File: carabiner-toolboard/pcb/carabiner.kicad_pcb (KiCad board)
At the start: 2 copper layers, 32.1 x 35.5 mm, 24 parts, among them J1 MF-Vertical 43045-1612, J2 MF-Horizontal 43045-1621, J7 MF-Horizontal 43045-1600

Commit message: Carabiner R1.1 - 'Who even needs more pins?'
Duplicates Aux3 - this allows you to wire up a BLTouch much easier
Increase the maximum ampere for PCFs to 2A total
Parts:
- added JP_Aux3: SolderJumper_2_Open, Jumper:SolderJumper-2_P1.3mm_Open_TrianglePad1.0x1.5mm, B.Cu at (76.4, 66.5)
- Probe1: footprint Connector_JST:JST_XH_B4B-XH-A_1x04_P2.50mm_Vertical -> Connector_JST:JST_XH_B5B-XH-A_1x05_P2.50mm_Vertical
- renumbered JP_HEF_Alt1 to HEF_Alt, JP_HEF_Main1 to HEF_Main, JP_PCF_Alt1 to PCF_Alt, JP_PCF_Main1 to PCF_Main
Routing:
- net A3: track 21.6 -> 30.7 mm
- net Net-(JP_Aux3-Pad2): track 0.00 -> 3.91 mm
- net PcFanGnd: track 23.3 -> 21.2 mm
- net PcFanSwitch: track 11.9 -> 10.9 mm
- net AltVolt: track 30.7 -> 30.3 mm, vias 1 -> 0
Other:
- board text added: "Carabiner R1.1"
- board text removed: "Carabiner R1.0.1"

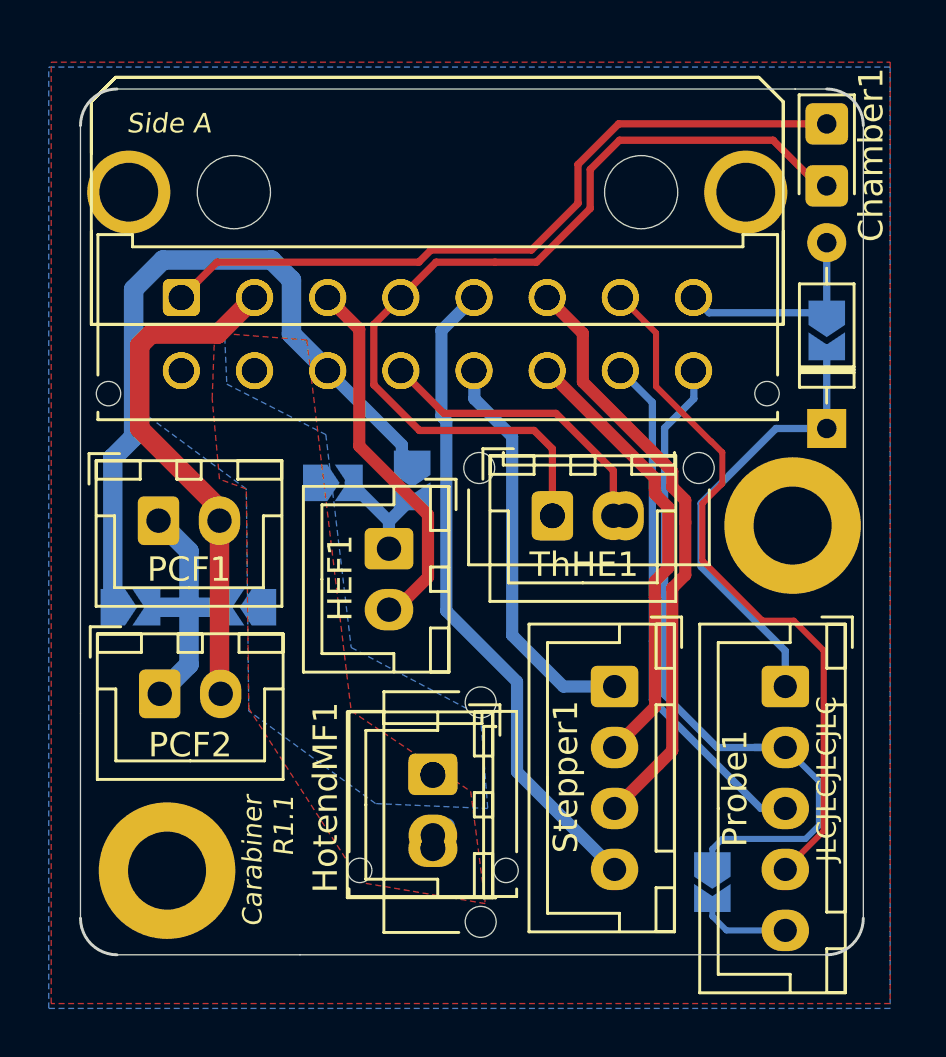
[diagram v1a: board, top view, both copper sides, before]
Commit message: Carabiner R 1.2 - Polishing it
- Renaming ports to fit the new unified naming scheme.
- Updated Readme to reflect that
- Support USB with the Aux ports! Use A2 and A3 for D+/D-
- Rework the motor trace routing
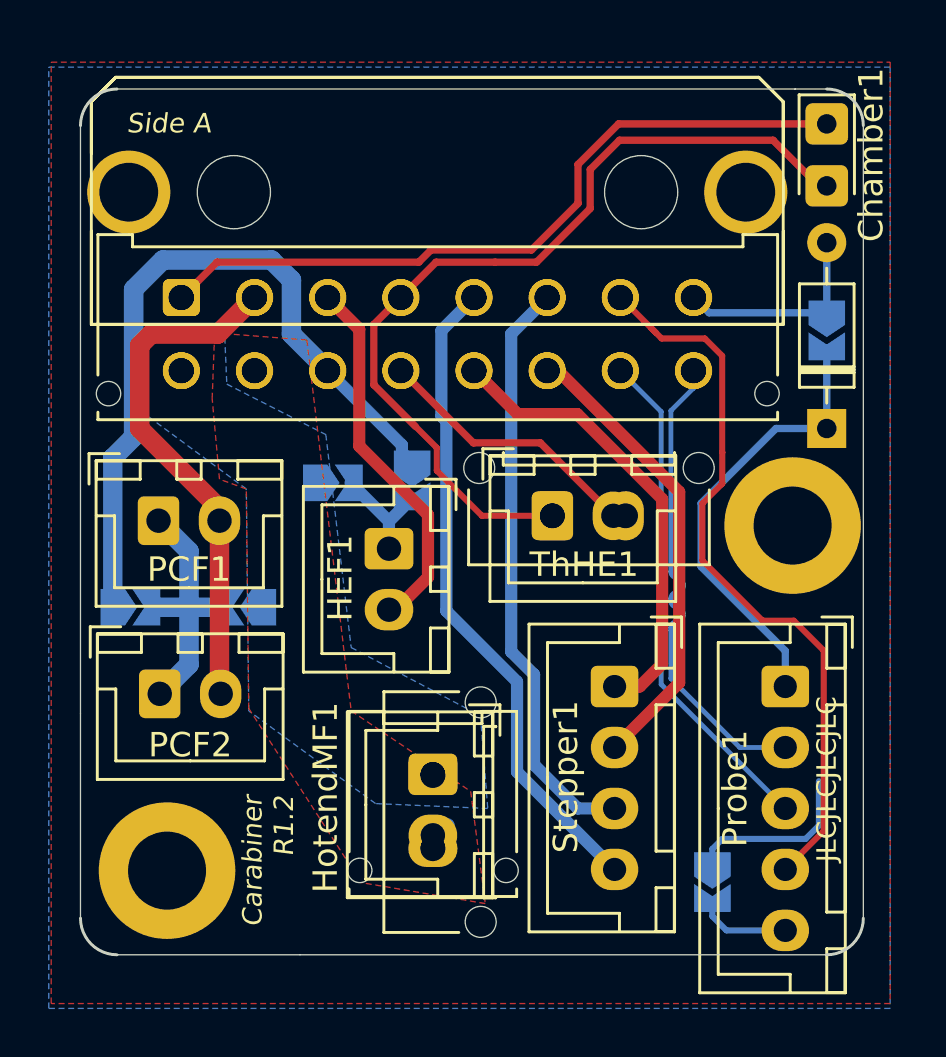
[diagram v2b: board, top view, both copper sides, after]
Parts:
- renumbered JPAux4 to JPA4, JP_Aux3 to JP_A3
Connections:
- net A2 renamed A2-
- net A3 renamed A2+
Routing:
- net A2+: track 30.7 -> 27.5 mm
- net Stepper2B: track 16.6 -> 19.0 mm
- net A1: track 29.0 -> 30.3 mm
- net ThHotend: track 13.4 -> 12.3 mm
- net ThCommonGnd: track 38.2 -> 37.2 mm
- net Stepper2A: track 18.9 -> 19.5 mm
- net A2-: track 21.3 -> 20.8 mm
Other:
- board text added: "1A"
- board text added: "1B"
- board text added: "2A"
- board text added: "2B"
- board text added: "A1"
- board text added: "A2"
- board text added: "A3"
- board text added: "A4"
- board text added: "Alt+"
- board text added: "Carabiner R1.2"
- board text added: "HEF-"
- board text added: "Main+"
- board text added: "PCF-"
- board text added: "ThChamb"
- board text removed: "AltVolt"
- board text removed: "Aux1"
- board text removed: "Aux2"
- board text removed: "Aux3"
- board text removed: "Aux4"
- board text removed: "Carabiner R1.1"
- board text removed: "HEFGnd"
- board text removed: "HeVolt"
- board text removed: "Main"
- board text removed: "MotorA"
- board text removed: "MotorB"
- board text removed: "MotorC"
- board text removed: "MotorD"
- board text removed: "PCFGnd"
- board text removed: "ThCham"
